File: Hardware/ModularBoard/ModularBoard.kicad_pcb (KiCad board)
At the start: 2 copper layers, 22.9 x 48.3 mm, 16 parts, among them IC1 WS2811-5050, IC2 WS2811-5050, IC3 WS2811-5050, IC4 WS2811-5050, IC5 ATTINY85-P, J1 GSG-USB-MICRO-B, K1 CONN_3, K2 CONN_3, K3 CONN_3, K4 CONN_3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

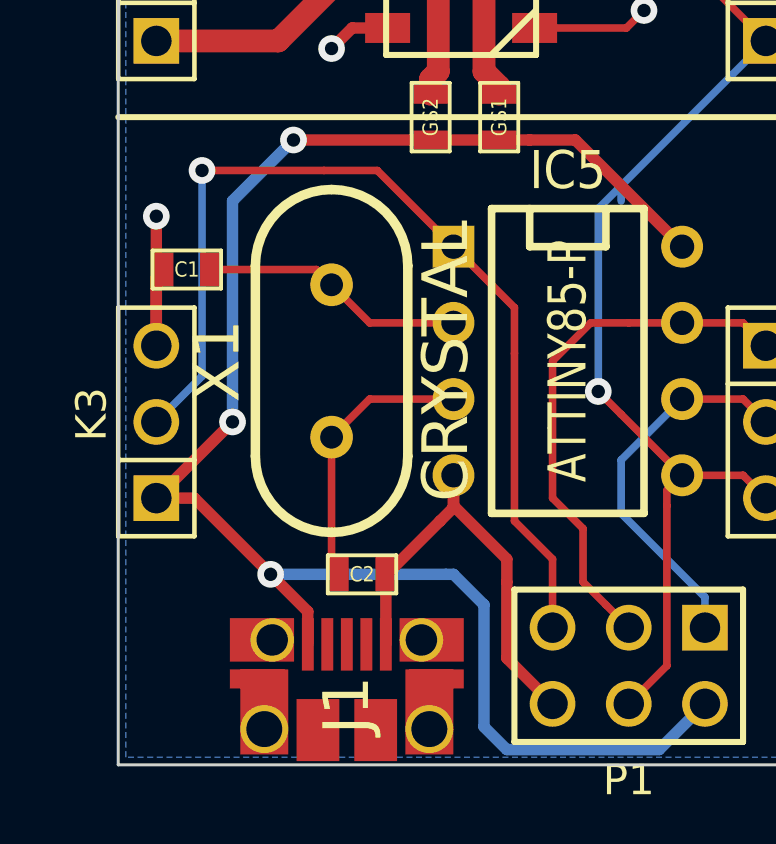
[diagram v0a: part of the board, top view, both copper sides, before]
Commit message: Switched crystal caps to 0805
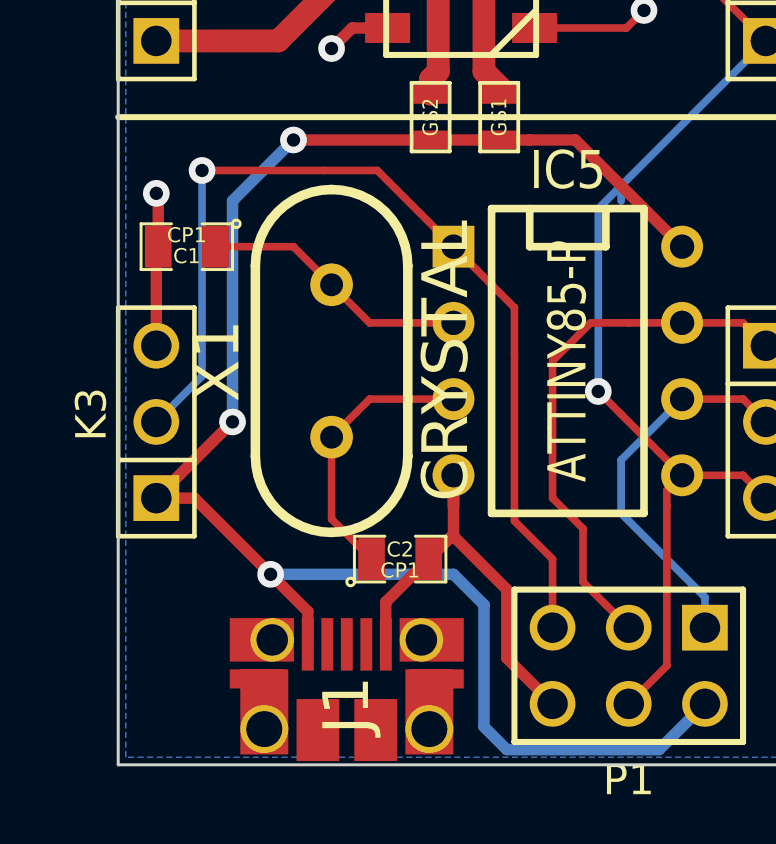
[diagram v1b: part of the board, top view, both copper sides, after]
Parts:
- C1, C2: footprint SM0603 -> SM0805
- moved C2 1.37 mm to (225.3, 160.8)
- moved C1 0.76 mm to (218.2, 150.4)
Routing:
- net GND: track 30.5 -> 28.8 mm
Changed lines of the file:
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@@
     (thickness 1.6)
     (drawings 5)
-    (tracks 168)
+    (tracks 170)
     (zones 0)
     (modules 16)
@@
     )
   )
-  (module SM0603 (layer F.Cu)
-    (at 218.186 151.13 180)
-    (attr smd)
-    (fp_text reference C1 (at 0 0 180) (layer F.SilkS)
-      (effects (font (size 0.508 0.4572) (thickness 0.1143)))
-    )
-    (fp_text value CP1 (at 0 0 180) (layer F.SilkS) hide
-      (effects (font (size 0.508 0.4572) (thickness 0.1143)))
-    )
-    (fp_line (start -1.143 -0.635) (end 1.143 -0.635) (layer F.SilkS) (width 0.127))
-    (fp_line (start 1.143 -0.635) (end 1.143 0.635) (layer F.SilkS) (width 0.127))
-    (fp_line (start 1.143 0.635) (end -1.143 0.635) (layer F.SilkS) (width 0.127))
-    (fp_line (start -1.143 0.635) (end -1.143 -0.635) (layer F.SilkS) (width 0.127))
-    (pad 1 smd rect (at -0.762 0 180) (size 0.635 1.143)
-      (layers F.Cu F.Paste F.Mask)
-      (net 10 N-0000017)
-    )
-    (pad 2 smd rect (at 0.762 0 180) (size 0.635 1.143)
-      (layers F.Cu F.Paste F.Mask)
-      (net 7 GND)
-    )
-    (model smd\resistors\R0603.wrl
-      (at (xyz 0 0 0.001))
-      (scale (xyz 0.5 0.5 0.5))
-      (rotate (xyz 0 0 0))
-    )
-  )
-  (module SM0603 (layer F.Cu)
-    (at 224.028 161.29)
-    (attr smd)
-    (fp_text reference C2 (at 0 0) (layer F.SilkS)
-      (effects (font (size 0.508 0.4572) (thickness 0.1143)))
-    )
-    (fp_text value CP1 (at 0 0) (layer F.SilkS) hide
-      (effects (font (size 0.508 0.4572) (thickness 0.1143)))
-    )
-    (fp_line (start -1.143 -0.635) (end 1.143 -0.635) (layer F.SilkS) (width 0.127))
-    (fp_line (start 1.143 -0.635) (end 1.143 0.635) (layer F.SilkS) (width 0.127))
-    (fp_line (start 1.143 0.635) (end -1.143 0.635) (layer F.SilkS) (width 0.127))
-    (fp_line (start -1.143 0.635) (end -1.143 -0.635) (layer F.SilkS) (width 0.127))
-    (pad 1 smd rect (at -0.762 0) (size 0.635 1.143)
-      (layers F.Cu F.Paste F.Mask)
-      (net 11 N-0000018)
-    )
-    (pad 2 smd rect (at 0.762 0) (size 0.635 1.143)
-      (layers F.Cu F.Paste F.Mask)
-      (net 7 GND)
-    )
-    (model smd\resistors\R0603.wrl
-      (at (xyz 0 0 0.001))
-      (scale (xyz 0.5 0.5 0.5))
-      (rotate (xyz 0 0 0))
-    )
-  )
   (module pin_array_3x2 (layer F.Cu)
     (at 232.918 164.338 180)
@@
       (at (xyz 0 0 0.001))
       (scale (xyz 0.5 0.5 0.5))
+      (rotate (xyz 0 0 0))
+    )
+  )
+  (module SM0805 (layer F.Cu)
+    (at 218.186 150.368 180)
+    (attr smd)
+    (fp_text reference C1 (at 0 -0.3175 180) (layer F.SilkS)
+      (effects (font (size 0.50038 0.50038) (thickness 0.10922)))
+    )
+    (fp_text value CP1 (at 0 0.381 180) (layer F.SilkS)
+      (effects (font (size 0.50038 0.50038) (thickness 0.10922)))
+    )
+    (fp_circle (center -1.651 0.762) (end -1.651 0.635) (layer F.SilkS) (width 0.09906))
+    (fp_line (start -0.508 0.762) (end -1.524 0.762) (layer F.SilkS) (width 0.09906))
+    (fp_line (start -1.524 0.762) (end -1.524 -0.762) (layer F.SilkS) (width 0.09906))
+    (fp_line (start -1.524 -0.762) (end -0.508 -0.762) (layer F.SilkS) (width 0.09906))
+    (fp_line (start 0.508 -0.762) (end 1.524 -0.762) (layer F.SilkS) (width 0.09906))
+    (fp_line (start 1.524 -0.762) (end 1.524 0.762) (layer F.SilkS) (width 0.09906))
+    (fp_line (start 1.524 0.762) (end 0.508 0.762) (layer F.SilkS) (width 0.09906))
+    (pad 1 smd rect (at -0.9525 0 180) (size 0.889 1.397)
+      (layers F.Cu F.Paste F.Mask)
+      (net 10 N-0000017)
+    )
+    (pad 2 smd rect (at 0.9525 0 180) (size 0.889 1.397)
+      (layers F.Cu F.Paste F.Mask)
+      (net 7 GND)
+    )
+    (model smd/chip_cms.wrl
+      (at (xyz 0 0 0))
+      (scale (xyz 0.1 0.1 0.1))
+      (rotate (xyz 0 0 0))
+    )
+  )
+  (module SM0805 (layer F.Cu)
+    (at 225.298 160.782)
+    (attr smd)
+    (fp_text reference C2 (at 0 -0.3175) (layer F.SilkS)
+      (effects (font (size 0.50038 0.50038) (thickness 0.10922)))
+    )
+    (fp_text value CP1 (at 0 0.381) (layer F.SilkS)
+      (effects (font (size 0.50038 0.50038) (thickness 0.10922)))
+    )
+    (fp_circle (center -1.651 0.762) (end -1.651 0.635) (layer F.SilkS) (width 0.09906))
+    (fp_line (start -0.508 0.762) (end -1.524 0.762) (layer F.SilkS) (width 0.09906))
+    (fp_line (start -1.524 0.762) (end -1.524 -0.762) (layer F.SilkS) (width 0.09906))
+    (fp_line (start -1.524 -0.762) (end -0.508 -0.762) (layer F.SilkS) (width 0.09906))
+    (fp_line (start 0.508 -0.762) (end 1.524 -0.762) (layer F.SilkS) (width 0.09906))
+    (fp_line (start 1.524 -0.762) (end 1.524 0.762) (layer F.SilkS) (width 0.09906))
+    (fp_line (start 1.524 0.762) (end 0.508 0.762) (layer F.SilkS) (width 0.09906))
+    (pad 1 smd rect (at -0.9525 0) (size 0.889 1.397)
+      (layers F.Cu F.Paste F.Mask)
+      (net 11 N-0000018)
+    )
+    (pad 2 smd rect (at 0.9525 0) (size 0.889 1.397)
+      (layers F.Cu F.Paste F.Mask)
+      (net 7 GND)
+    )
+    (model smd/chip_cms.wrl
+      (at (xyz 0 0 0))
+      (scale (xyz 0.1 0.1 0.1))
       (rotate (xyz 0 0 0))
     )
@@
   (segment (start 234.696 152.908) (end 236.728 152.908) (width 0.254) (layer F.Cu) (net 6))
   (segment (start 236.728 152.908) (end 237.49 153.67) (width 0.254) (layer F.Cu) (net 6))
+  (segment (start 217.2335 150.368) (end 217.2335 148.6535) (width 0.381) (layer F.Cu) (net 7) (status 400000))
+  (via (at 217.17 148.59) (size 0.889) (layers F.Cu B.Cu) (net 7))
+  (segment (start 217.2335 148.6535) (end 217.17 148.59) (width 0.381) (layer F.Cu) (net 7))
+  (segment (start 217.17 153.67) (end 217.17 150.4315) (width 0.381) (layer F.Cu) (net 7) (status C00000))
+  (segment (start 217.17 150.4315) (end 217.2335 150.368) (width 0.381) (layer F.Cu) (net 7) (status C00000))
+  (segment (start 227.076 159.9565) (end 227.076 160.02) (width 0.381) (layer F.Cu) (net 7))
+  (segment (start 228.854 164.084) (end 230.378 165.608) (width 0.381) (layer F.Cu) (net 7))
+  (segment (start 228.854 161.798) (end 228.854 164.084) (width 0.381) (layer F.Cu) (net 7))
+  (segment (start 227.076 160.02) (end 228.854 161.798) (width 0.381) (layer F.Cu) (net 7))
+  (segment (start 227.076 157.988) (end 227.076 159.9565) (width 0.381) (layer F.Cu) (net 7))
+  (segment (start 227.076 159.9565) (end 226.2505 160.782) (width 0.381) (layer F.Cu) (net 7))
+  (segment (start 224.82048 163.62426) (end 224.82048 162.21202) (width 0.381) (layer F.Cu) (net 7))
+  (segment (start 224.82048 162.21202) (end 226.2505 160.782) (width 0.381) (layer F.Cu) (net 7))
   (segment (start 227.076 157.988) (end 227.076 159.004) (width 0.381) (layer F.Cu) (net 7))
-  (segment (start 228.854 161.544) (end 228.854 164.084) (width 0.381) (layer F.Cu) (net 7))
-  (segment (start 228.854 164.084) (end 230.378 165.608) (width 0.381) (layer F.Cu) (net 7))
-  (segment (start 228.854 160.782) (end 228.854 161.544) (width 0.381) (layer F.Cu) (net 7))
-  (segment (start 227.076 159.004) (end 228.854 160.782) (width 0.381) (layer F.Cu) (net 7))
   (segment (start 227.076 157.988) (end 227.076 159.06496) (width 0.381) (layer F.Cu) (net 7))
-  (segment (start 224.82048 161.32048) (end 226.62896 159.512) (width 0.381) (layer F.Cu) (net 7))
-  (segment (start 224.82048 161.32048) (end 224.82048 163.62426) (width 0.381) (layer F.Cu) (net 7))
-  (segment (start 227.076 159.06496) (end 226.62896 159.512) (width 0.381) (layer F.Cu) (net 7))
-  (segment (start 217.17 153.67) (end 217.17 149.352) (width 0.381) (layer F.Cu) (net 7))
-  (via (at 217.17 149.352) (size 0.889) (layers F.Cu B.Cu) (net 7))
   (segment (start 224.88 124.79) (end 223.19 124.79) (width 0.381) (layer F.Cu) (net 7))
   (via (at 223.012 124.968) (size 0.889) (layers F.Cu B.Cu) (net 7))
@@
   (via (at 223.012 143.764) (size 0.889) (layers F.Cu B.Cu) (net 7))
   (segment (start 223.698 143.078) (end 223.012 143.764) (width 0.381) (layer F.Cu) (net 7))
-  (segment (start 217.17 153.67) (end 217.17 151.384) (width 0.381) (layer F.Cu) (net 7))
-  (segment (start 217.17 151.384) (end 217.424 151.13) (width 0.381) (layer F.Cu) (net 7))
   (segment (start 233.426 135.382) (end 233.426 130.81) (width 0.254) (layer F.Cu) (net 8))
   (segment (start 231.826 136.982) (end 231.902 136.906) (width 0.254) (layer F.Cu) (net 8))
@@
   (segment (start 231.826 130.886) (end 229.78 130.886) (width 0.254) (layer F.Cu) (net 9))
   (segment (start 233.426 124.714) (end 231.902 123.19) (width 0.254) (layer F.Cu) (net 9))
+  (segment (start 219.1385 150.368) (end 221.742 150.368) (width 0.254) (layer F.Cu) (net 10) (status 400000))
+  (segment (start 221.742 150.368) (end 223.012 151.638) (width 0.254) (layer F.Cu) (net 10) (status 800000))
   (segment (start 227.076 152.908) (end 224.282 152.908) (width 0.254) (layer F.Cu) (net 10))
   (segment (start 224.282 152.908) (end 223.012 151.638) (width 0.254) (layer F.Cu) (net 10))
-  (segment (start 218.948 151.13) (end 222.504 151.13) (width 0.254) (layer F.Cu) (net 10))
-  (segment (start 222.504 151.13) (end 223.012 151.638) (width 0.254) (layer F.Cu) (net 10))
+  (segment (start 223.012 156.718) (end 223.012 159.4485) (width 0.254) (layer F.Cu) (net 11))
+  (segment (start 223.012 159.4485) (end 224.3455 160.782) (width 0.254) (layer F.Cu) (net 11))
   (segment (start 227.076 155.448) (end 224.282 155.448) (width 0.254) (layer F.Cu) (net 11))
   (segment (start 224.282 155.448) (end 223.012 156.718) (width 0.254) (layer F.Cu) (net 11))
-  (segment (start 223.012 156.718) (end 223.012 161.036) (width 0.254) (layer F.Cu) (net 11))
-  (segment (start 223.012 161.036) (end 223.266 161.29) (width 0.254) (layer F.Cu) (net 11))
   (segment (start 231.902 135.382) (end 233.426 136.906) (width 0.254) (layer F.Cu) (net 12))
   (segment (start 229.78 135.382) (end 231.902 135.382) (width 0.254) (layer F.Cu) (net 12))

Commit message: Rendered gerber files, ordered from OSHPark!
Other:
- board text added: "Made with Love for Alexx by Mark"
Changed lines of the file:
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@@
     (area 214.1728 117.33529 240.4872 178.75504)
     (thickness 1.6)
-    (drawings 5)
+    (drawings 6)
     (tracks 170)
     (zones 0)
@@
     (visible_elements 7FFFFFFF)
     (pcbplotparams
-      (layerselection 3178497)
+      (layerselection 2097152)
       (usegerberextensions true)
       (excludeedgelayer true)
@@
       (outputformat 1)
       (mirror false)
-      (drillshape 1)
+      (drillshape 0)
       (scaleselection 1)
-      (outputdirectory ""))
+      (outputdirectory GerberFiles/))
   )
   (net 0 "")
@@
     (descr "Double rangee de contacts 2 x 4 pins")
     (tags CONN)
-    (fp_text reference P1 (at 0 -3.81 180) (layer F.SilkS)
+    (fp_text reference P1 (at 0 3.556 180) (layer F.SilkS)
       (effects (font (size 1.016 1.016) (thickness 0.2032)))
     )
@@
     (descr "Connecteur 3 pins")
     (tags "CONN DEV")
-    (fp_text reference K2 (at 0.254 -2.159 90) (layer F.SilkS)
+    (fp_text reference K2 (at 5.08 -0.254 90) (layer F.SilkS)
       (effects (font (size 1.016 1.016) (thickness 0.1524)))
     )
@@
     (descr "Connecteur 3 pins")
     (tags "CONN DEV")
-    (fp_text reference K1 (at 0.254 -2.159 270) (layer F.SilkS)
+    (fp_text reference K1 (at -5.08 -0.508 270) (layer F.SilkS)
       (effects (font (size 1.016 1.016) (thickness 0.1524)))
     )
@@
     (descr "Connecteur 3 pins")
     (tags "CONN DEV")
-    (fp_text reference K3 (at 0.254 -2.159 90) (layer F.SilkS)
+    (fp_text reference K3 (at -5.08 -0.254 90) (layer F.SilkS)
       (effects (font (size 1.016 1.016) (thickness 0.1524)))
     )
@@
     (descr "Connecteur 3 pins")
     (tags "CONN DEV")
-    (fp_text reference K4 (at 0.254 -2.159 90) (layer F.SilkS)
+    (fp_text reference K4 (at 5.08 0.508 90) (layer F.SilkS)
       (effects (font (size 1.016 1.016) (thickness 0.1524)))
     )
@@
       (rotate (xyz 0 0 0))
     )
+  )
+  (gr_text "Made with Love\nfor Alexx by Mark" (at 230.378 154.178 90) (layer B.SilkS)
+    (effects (font (size 0.762 0.762) (thickness 0.127)) (justify mirror))
   )
   (gr_line (start 238.76 146.05) (end 215.9 146.05) (angle 90) (layer F.SilkS) (width 0.2))
@@
   (segment (start 234.696 152.908) (end 236.728 152.908) (width 0.254) (layer F.Cu) (net 6))
   (segment (start 236.728 152.908) (end 237.49 153.67) (width 0.254) (layer F.Cu) (net 6))
-  (segment (start 217.2335 150.368) (end 217.2335 148.6535) (width 0.381) (layer F.Cu) (net 7) (status 400000))
+  (segment (start 217.2335 150.368) (end 217.2335 148.6535) (width 0.381) (layer F.Cu) (net 7))
   (via (at 217.17 148.59) (size 0.889) (layers F.Cu B.Cu) (net 7))
   (segment (start 217.2335 148.6535) (end 217.17 148.59) (width 0.381) (layer F.Cu) (net 7))
-  (segment (start 217.17 153.67) (end 217.17 150.4315) (width 0.381) (layer F.Cu) (net 7) (status C00000))
-  (segment (start 217.17 150.4315) (end 217.2335 150.368) (width 0.381) (layer F.Cu) (net 7) (status C00000))
+  (segment (start 217.17 153.67) (end 217.17 150.4315) (width 0.381) (layer F.Cu) (net 7))
+  (segment (start 217.17 150.4315) (end 217.2335 150.368) (width 0.381) (layer F.Cu) (net 7))
   (segment (start 227.076 159.9565) (end 227.076 160.02) (width 0.381) (layer F.Cu) (net 7))
   (segment (start 228.854 164.084) (end 230.378 165.608) (width 0.381) (layer F.Cu) (net 7))
@@
   (segment (start 231.826 130.886) (end 229.78 130.886) (width 0.254) (layer F.Cu) (net 9))
   (segment (start 233.426 124.714) (end 231.902 123.19) (width 0.254) (layer F.Cu) (net 9))
-  (segment (start 219.1385 150.368) (end 221.742 150.368) (width 0.254) (layer F.Cu) (net 10) (status 400000))
-  (segment (start 221.742 150.368) (end 223.012 151.638) (width 0.254) (layer F.Cu) (net 10) (status 800000))
+  (segment (start 219.1385 150.368) (end 221.742 150.368) (width 0.254) (layer F.Cu) (net 10))
+  (segment (start 221.742 150.368) (end 223.012 151.638) (width 0.254) (layer F.Cu) (net 10))
   (segment (start 227.076 152.908) (end 224.282 152.908) (width 0.254) (layer F.Cu) (net 10))
   (segment (start 224.282 152.908) (end 223.012 151.638) (width 0.254) (layer F.Cu) (net 10))
